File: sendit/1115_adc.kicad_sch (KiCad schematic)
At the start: 4 parts, among them U1 ADS1115IDGS

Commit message: big update on the potential design.
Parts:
- renumbered C1 to C2, C2 to C3, R2 to R6, U1 to U2
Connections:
- net +5V renamed +3.3V
- net GNDA renamed GND
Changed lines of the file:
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@@
 				)
 				(justify left)
-				(hide yes)
 			)
 		)
@@
 				)
 				(justify left)
-				(hide yes)
 			)
 		)
@@
 		(on_board yes)
 		(dnp no)
-		(property "Reference" "C2"
+		(property "Reference" "C3"
 			(at 176.53 88.9063 0)
 			(effects
@@
 		(instances
 			(project "sendit"
-				(path "/a355e4d0-2918-44fc-be8d-2503b84c6d6c/b74372e1-8e8c-456e-860f-c00883d6d009"
-					(reference "C4")
+				(path "/a355e4d0-2918-44fc-be8d-2503b84c6d6c/3be26641-bb38-49f4-a8c8-35d985e646a7"
+					(reference "C3")
 					(unit 1)
 				)
 				(path "/a355e4d0-2918-44fc-be8d-2503b84c6d6c/d44ed8a4-b2b5-49ad-a2f4-3423c838bfc7"
-					(reference "C2")
+					(reference "C8")
+					(unit 1)
+				)
+			)
+		)
+	)
+	(symbol
+		(lib_id "power:GND")
+		(at 132.08 107.95 0)
+		(unit 1)
+		(exclude_from_sim no)
+		(in_bom yes)
+		(on_board yes)
+		(dnp no)
+		(fields_autoplaced yes)
+		(property "Reference" "#PWR012"
+			(at 132.08 114.3 0)
+			(effects
+				(font
+					(size 1.27 1.27)
+				)
+				(hide yes)
+			)
+		)
+		(property "Value" "GND"
+			(at 132.08 113.03 0)
+			(effects
+				(font
+					(size 1.27 1.27)
+				)
+			)
+		)
+		(property "Footprint" ""
+			(at 132.08 107.95 0)
+			(effects
+				(font
+					(size 1.27 1.27)
+				)
+				(hide yes)
+			)
+		)
+		(property "Datasheet" ""
+			(at 132.08 107.95 0)
+			(effects
+				(font
+					(size 1.27 1.27)
+				)
+				(hide yes)
+			)
+		)
+		(property "Description" "Power symbol creates a global label with name \"GND\" , ground"
+			(at 132.08 107.95 0)
+			(effects
+				(font
+					(size 1.27 1.27)
+				)
+				(hide yes)
+			)
+		)
+		(pin "1"
+		)
+		(instances
+			(project "sendit"
+				(path "/a355e4d0-2918-44fc-be8d-2503b84c6d6c/3be26641-bb38-49f4-a8c8-35d985e646a7"
+					(reference "#PWR012")
+					(unit 1)
+				)
+				(path "/a355e4d0-2918-44fc-be8d-2503b84c6d6c/d44ed8a4-b2b5-49ad-a2f4-3423c838bfc7"
+					(reference "#PWR030")
 					(unit 1)
 				)
@@
 		(on_board yes)
 		(dnp no)
-		(property "Reference" "C1"
+		(property "Reference" "C2"
 			(at 163.83 88.9063 0)
 			(effects
@@
 		(instances
 			(project "sendit"
-				(path "/a355e4d0-2918-44fc-be8d-2503b84c6d6c/b74372e1-8e8c-456e-860f-c00883d6d009"
-					(reference "C3")
+				(path "/a355e4d0-2918-44fc-be8d-2503b84c6d6c/3be26641-bb38-49f4-a8c8-35d985e646a7"
+					(reference "C2")
 					(unit 1)
 				)
 				(path "/a355e4d0-2918-44fc-be8d-2503b84c6d6c/d44ed8a4-b2b5-49ad-a2f4-3423c838bfc7"
-					(reference "C1")
+					(reference "C7")
 					(unit 1)
 				)
@@
 		(dnp no)
 		(fields_autoplaced yes)
-		(property "Reference" "R2"
+		(property "Reference" "R6"
 			(at 153.67 81.28 0)
 			(effects
@@
 		(instances
 			(project "sendit"
-				(path "/a355e4d0-2918-44fc-be8d-2503b84c6d6c/b74372e1-8e8c-456e-860f-c00883d6d009"
-					(reference "R10")
+				(path "/a355e4d0-2918-44fc-be8d-2503b84c6d6c/3be26641-bb38-49f4-a8c8-35d985e646a7"
+					(reference "R6")
 					(unit 1)
 				)
 				(path "/a355e4d0-2918-44fc-be8d-2503b84c6d6c/d44ed8a4-b2b5-49ad-a2f4-3423c838bfc7"
-					(reference "R2")
+					(reference "R12")
 					(unit 1)
 				)
@@
 		(dnp no)
 		(fields_autoplaced yes)
-		(property "Reference" "U1"
+		(property "Reference" "U2"
 			(at 134.2741 80.01 0)
 			(effects
@@
 		(instances
 			(project "sendit"
-				(path "/a355e4d0-2918-44fc-be8d-2503b84c6d6c/b74372e1-8e8c-456e-860f-c00883d6d009"
-					(reference "U3")
+				(path "/a355e4d0-2918-44fc-be8d-2503b84c6d6c/3be26641-bb38-49f4-a8c8-35d985e646a7"
+					(reference "U2")
 					(unit 1)
 				)
 				(path "/a355e4d0-2918-44fc-be8d-2503b84c6d6c/d44ed8a4-b2b5-49ad-a2f4-3423c838bfc7"
-					(reference "U1")
+					(reference "U4")
 					(unit 1)
 				)
@@
 	)
 	(symbol
-		(lib_id "power:GNDA")
-		(at 132.08 107.95 0)
-		(unit 1)
-		(exclude_from_sim no)
-		(in_bom yes)
-		(on_board yes)
-		(dnp no)
-		(property "Reference" "#PWR03"
-			(at 132.08 114.3 0)
-			(effects
-				(font
-					(size 1.27 1.27)
-				)
-				(hide yes)
-			)
-		)
-		(property "Value" "GNDA"
-			(at 132.08 111.76 0)
-			(effects
-				(font
-					(size 1.27 1.27)
-				)
-			)
-		)
-		(property "Footprint" ""
-			(at 132.08 107.95 0)
-			(effects
-				(font
-					(size 1.27 1.27)
-				)
-				(hide yes)
-			)
-		)
-		(property "Datasheet" ""
-			(at 132.08 107.95 0)
-			(effects
-				(font
-					(size 1.27 1.27)
-				)
-				(hide yes)
-			)
-		)
-		(property "Description" "Power symbol creates a global label with name \"GNDA\" , analog ground"
-			(at 132.08 107.95 0)
-			(effects
-				(font
-					(size 1.27 1.27)
-				)
-				(hide yes)
-			)
-		)
-		(pin "1"
-		)
-		(instances
-			(project "sendit"
-				(path "/a355e4d0-2918-44fc-be8d-2503b84c6d6c/b74372e1-8e8c-456e-860f-c00883d6d009"
-					(reference "#PWR022")
-					(unit 1)
-				)
-				(path "/a355e4d0-2918-44fc-be8d-2503b84c6d6c/d44ed8a4-b2b5-49ad-a2f4-3423c838bfc7"
-					(reference "#PWR03")
-					(unit 1)
-				)
-			)
-		)
-	)
-	(symbol
-		(lib_id "power:+5V")
+		(lib_id "power:+3.3V")
 		(at 132.08 72.39 0)
 		(unit 1)
@@
 		(dnp no)
 		(fields_autoplaced yes)
-		(property "Reference" "#PWR02"
+		(property "Reference" "#PWR011"
 			(at 132.08 76.2 0)
 			(effects
@@
 			)
 		)
-		(property "Value" "+5V"
+		(property "Value" "+3.3V"
 			(at 132.08 67.31 0)
 			(effects
@@
 			)
 		)
-		(property "Description" "Power symbol creates a global label with name \"+5V\""
+		(property "Description" "Power symbol creates a global label with name \"+3.3V\""
 			(at 132.08 72.39 0)
 			(effects
@@
 		(instances
 			(project "sendit"
-				(path "/a355e4d0-2918-44fc-be8d-2503b84c6d6c/b74372e1-8e8c-456e-860f-c00883d6d009"
-					(reference "#PWR021")
+				(path "/a355e4d0-2918-44fc-be8d-2503b84c6d6c/3be26641-bb38-49f4-a8c8-35d985e646a7"
+					(reference "#PWR011")
 					(unit 1)
 				)
 				(path "/a355e4d0-2918-44fc-be8d-2503b84c6d6c/d44ed8a4-b2b5-49ad-a2f4-3423c838bfc7"
-					(reference "#PWR02")
-					(unit 1)
-				)
+					(reference "#PWR029")
+					(unit 1)
+				)

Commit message: layout work.
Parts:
- renumbered R6 to R9
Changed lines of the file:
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@@
 				)
 				(path "/a355e4d0-2918-44fc-be8d-2503b84c6d6c/d44ed8a4-b2b5-49ad-a2f4-3423c838bfc7"
-					(reference "C8")
+					(reference "C7")
 					(unit 1)
 				)
@@
 		(dnp no)
 		(fields_autoplaced yes)
-		(property "Reference" "#PWR012"
+		(property "Reference" "#PWR019"
 			(at 132.08 114.3 0)
 			(effects
@@
 			(project "sendit"
 				(path "/a355e4d0-2918-44fc-be8d-2503b84c6d6c/3be26641-bb38-49f4-a8c8-35d985e646a7"
-					(reference "#PWR012")
-					(unit 1)
-				)
-				(path "/a355e4d0-2918-44fc-be8d-2503b84c6d6c/d44ed8a4-b2b5-49ad-a2f4-3423c838bfc7"
-					(reference "#PWR030")
+					(reference "#PWR019")
+					(unit 1)
+				)
+				(path "/a355e4d0-2918-44fc-be8d-2503b84c6d6c/d44ed8a4-b2b5-49ad-a2f4-3423c838bfc7"
+					(reference "#PWR043")
 					(unit 1)
 				)
@@
 				)
 				(path "/a355e4d0-2918-44fc-be8d-2503b84c6d6c/d44ed8a4-b2b5-49ad-a2f4-3423c838bfc7"
-					(reference "C7")
+					(reference "C6")
 					(unit 1)
 				)
@@
 		(dnp no)
 		(fields_autoplaced yes)
-		(property "Reference" "R6"
+		(property "Reference" "R9"
 			(at 153.67 81.28 0)
 			(effects
@@
 			(project "sendit"
 				(path "/a355e4d0-2918-44fc-be8d-2503b84c6d6c/3be26641-bb38-49f4-a8c8-35d985e646a7"
-					(reference "R6")
-					(unit 1)
-				)
-				(path "/a355e4d0-2918-44fc-be8d-2503b84c6d6c/d44ed8a4-b2b5-49ad-a2f4-3423c838bfc7"
-					(reference "R12")
+					(reference "R9")
+					(unit 1)
+				)
+				(path "/a355e4d0-2918-44fc-be8d-2503b84c6d6c/d44ed8a4-b2b5-49ad-a2f4-3423c838bfc7"
+					(reference "R26")
 					(unit 1)
 				)
@@
 				)
 				(path "/a355e4d0-2918-44fc-be8d-2503b84c6d6c/d44ed8a4-b2b5-49ad-a2f4-3423c838bfc7"
-					(reference "U4")
+					(reference "U3")
 					(unit 1)
 				)
@@
 		(dnp no)
 		(fields_autoplaced yes)
-		(property "Reference" "#PWR011"
+		(property "Reference" "#PWR018"
 			(at 132.08 76.2 0)
 			(effects
@@
 			(project "sendit"
 				(path "/a355e4d0-2918-44fc-be8d-2503b84c6d6c/3be26641-bb38-49f4-a8c8-35d985e646a7"
-					(reference "#PWR011")
-					(unit 1)
-				)
-				(path "/a355e4d0-2918-44fc-be8d-2503b84c6d6c/d44ed8a4-b2b5-49ad-a2f4-3423c838bfc7"
-					(reference "#PWR029")
-					(unit 1)
-				)
+					(reference "#PWR018")
+					(unit 1)
+				)
+				(path "/a355e4d0-2918-44fc-be8d-2503b84c6d6c/d44ed8a4-b2b5-49ad-a2f4-3423c838bfc7"
+					(reference "#PWR042")
+					(unit 1)
+				)

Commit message: updated footprints and lcsc numbers.
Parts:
- C2: footprint Capacitor_SMD:C_0805_2012Metric_Pad1.18x1.45mm_HandSolder -> Capacitor_SMD:C_0603_1608Metric; LCSC C49678 -> C14663
- C3: footprint Capacitor_SMD:C_0805_2012Metric_Pad1.18x1.45mm_HandSolder -> Capacitor_SMD:C_0603_1608Metric; LCSC C1952580 -> C19702
- R9: footprint Resistor_SMD:R_0805_2012Metric_Pad1.20x1.40mm_HandSolder -> Resistor_SMD:R_0603_1608Metric; LCSC C84376 -> (none)
- U2: LCSC (none) -> C37593
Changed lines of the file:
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@@
 			)
 		)
-		(property "Footprint" "Capacitor_SMD:C_0805_2012Metric_Pad1.18x1.45mm_HandSolder"
+		(property "Footprint" "Capacitor_SMD:C_0603_1608Metric"
 			(at 173.99 90.17 0)
 			(effects
@@
 			)
 		)
-		(property "LCSC" "C1952580"
+		(property "LCSC" "C19702"
 			(at 173.99 90.17 0)
 			(effects
@@
 			)
 		)
-		(property "Footprint" "Capacitor_SMD:C_0805_2012Metric_Pad1.18x1.45mm_HandSolder"
+		(property "Footprint" "Capacitor_SMD:C_0603_1608Metric"
 			(at 161.29 90.17 0)
 			(effects
@@
 			)
 		)
-		(property "LCSC" "C49678"
+		(property "LCSC" "C14663"
 			(at 161.29 90.17 0)
 			(effects
@@
 			)
 		)
-		(property "Footprint" "Resistor_SMD:R_0805_2012Metric_Pad1.20x1.40mm_HandSolder"
+		(property "Footprint" "Resistor_SMD:R_0603_1608Metric"
 			(at 151.13 82.55 0)
 			(effects
@@
 			)
 		)
-		(property "LCSC" "C84376"
+		(property "LCSC" ""
 			(at 151.13 82.55 0)
 			(effects
@@
 			)
 		)
-		(property "LCSC" ""
+		(property "LCSC" "C37593"
 			(at 132.08 95.25 0)
 			(effects

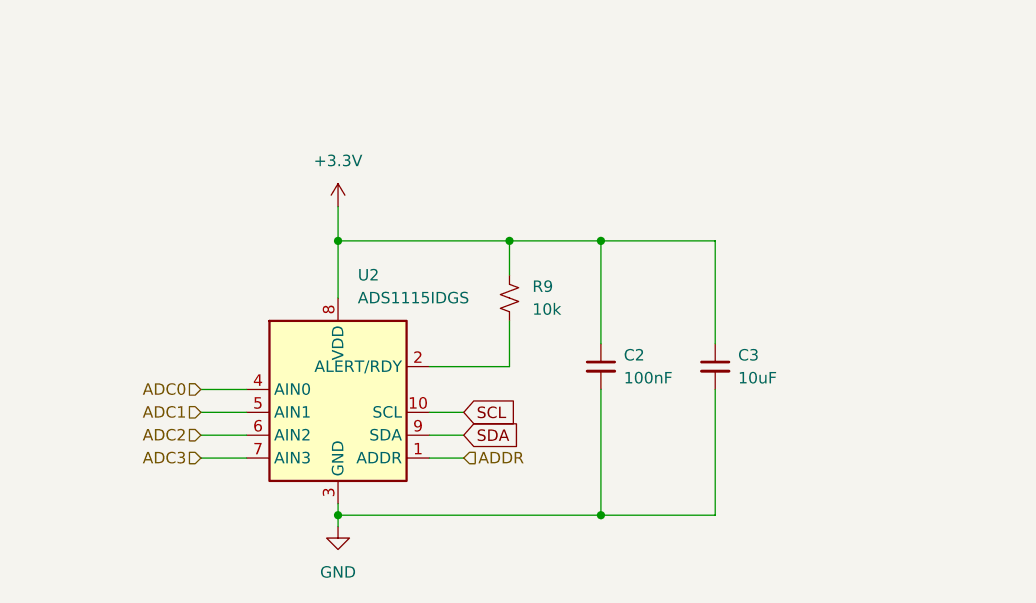
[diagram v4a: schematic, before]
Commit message: test run of jlcpcb upload looks good.
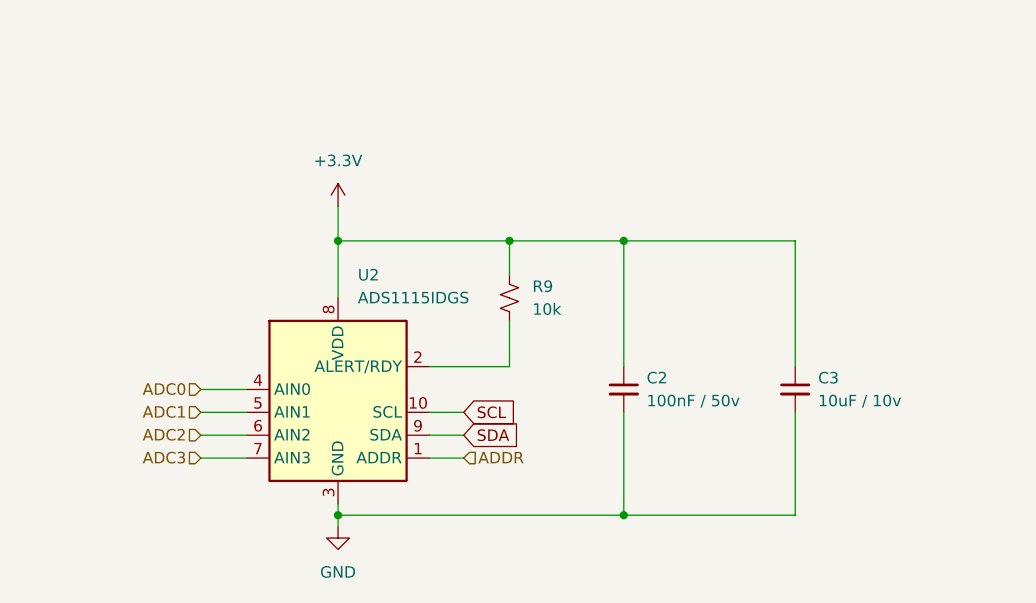
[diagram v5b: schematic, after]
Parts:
- C2: value 100nF -> 100nF / 50v
- C3: value 10uF -> 10uF / 10v
- R9: LCSC (none) -> C25804
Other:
- moved on the sheet: C2, C3
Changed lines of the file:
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@@
 	)
 	(junction
-		(at 161.29 106.68)
+		(at 163.83 106.68)
 		(diameter 0)
 		(color 0 0 0 0)
 	)
 	(junction
-		(at 161.29 76.2)
+		(at 163.83 76.2)
 		(diameter 0)
 		(color 0 0 0 0)
@@
 	(wire
 		(pts
-			(xy 161.29 106.68) (xy 132.08 106.68)
+			(xy 132.08 106.68) (xy 163.83 106.68)
 		)
 		(stroke
@@
 	(wire
 		(pts
-			(xy 161.29 76.2) (xy 173.99 76.2)
-		)
-		(stroke
-			(width 0)
-			(type default)
-		)
-	)
-	(wire
-		(pts
 			(xy 116.84 97.79) (xy 121.92 97.79)
 		)
@@
 	(wire
 		(pts
-			(xy 173.99 106.68) (xy 161.29 106.68)
+			(xy 182.88 106.68) (xy 163.83 106.68)
 		)
 		(stroke
@@
 	(wire
 		(pts
-			(xy 161.29 92.71) (xy 161.29 106.68)
+			(xy 163.83 95.25) (xy 163.83 106.68)
 		)
 		(stroke
@@
 	(wire
 		(pts
-			(xy 173.99 92.71) (xy 173.99 106.68)
-		)
-		(stroke
-			(width 0)
-			(type default)
-		)
-	)
-	(wire
-		(pts
-			(xy 151.13 76.2) (xy 161.29 76.2)
+			(xy 182.88 95.25) (xy 182.88 106.68)
+		)
+		(stroke
+			(width 0)
+			(type default)
+		)
+	)
+	(wire
+		(pts
+			(xy 151.13 76.2) (xy 163.83 76.2)
 		)
 		(stroke
@@
 	(wire
 		(pts
-			(xy 161.29 76.2) (xy 161.29 87.63)
-		)
-		(stroke
-			(width 0)
-			(type default)
-		)
-	)
-	(wire
-		(pts
-			(xy 173.99 76.2) (xy 173.99 87.63)
+			(xy 163.83 76.2) (xy 163.83 90.17)
+		)
+		(stroke
+			(width 0)
+			(type default)
+		)
+	)
+	(wire
+		(pts
+			(xy 182.88 76.2) (xy 182.88 90.17)
 		)
 		(stroke
@@
 		(pts
 			(xy 142.24 90.17) (xy 151.13 90.17)
+		)
+		(stroke
+			(width 0)
+			(type default)
+		)
+	)
+	(wire
+		(pts
+			(xy 163.83 76.2) (xy 182.88 76.2)
 		)
 		(stroke
@@
 	(symbol
 		(lib_id "Device:C_Small")
-		(at 173.99 90.17 0)
+		(at 182.88 92.71 0)
 		(unit 1)
 		(exclude_from_sim no)
@@
 		(dnp no)
 		(property "Reference" "C3"
-			(at 176.53 88.9063 0)
+			(at 185.42 91.4463 0)
 			(effects
 				(font
@@
 			)
 		)
-		(property "Value" "10uF"
-			(at 176.53 91.4463 0)
+		(property "Value" "10uF / 10v"
+			(at 185.42 93.9863 0)
 			(effects
 				(font
@@
 		)
 		(property "Footprint" "Capacitor_SMD:C_0603_1608Metric"
-			(at 173.99 90.17 0)
+			(at 182.88 92.71 0)
 			(effects
 				(font
@@
 		)
 		(property "Datasheet" "~"
-			(at 173.99 90.17 0)
+			(at 182.88 92.71 0)
 			(effects
 				(font
@@
 		)
 		(property "Description" ""
-			(at 173.99 90.17 0)
+			(at 182.88 92.71 0)
 			(effects
 				(font
@@
 		)
 		(property "Vendor" ""
-			(at 173.99 90.17 0)
+			(at 182.88 92.71 0)
 			(effects
 				(font
@@
 		)
 		(property "LCSC" "C19702"
-			(at 173.99 90.17 0)
+			(at 182.88 92.71 0)
 			(effects
 				(font
@@
 	(symbol
 		(lib_id "Device:C_Small")
-		(at 161.29 90.17 0)
+		(at 163.83 92.71 0)
 		(unit 1)
 		(exclude_from_sim no)
@@
 		(dnp no)
 		(property "Reference" "C2"
-			(at 163.83 88.9063 0)
+			(at 166.37 91.4463 0)
 			(effects
 				(font
@@
 			)
 		)
-		(property "Value" "100nF"
-			(at 163.83 91.4463 0)
+		(property "Value" "100nF / 50v"
+			(at 166.37 93.9863 0)
 			(effects
 				(font
@@
 		)
 		(property "Footprint" "Capacitor_SMD:C_0603_1608Metric"
-			(at 161.29 90.17 0)
+			(at 163.83 92.71 0)
 			(effects
 				(font
@@
 		)
 		(property "Datasheet" "~"
-			(at 161.29 90.17 0)
+			(at 163.83 92.71 0)
 			(effects
 				(font
@@
 		)
 		(property "Description" ""
-			(at 161.29 90.17 0)
+			(at 163.83 92.71 0)
 			(effects
 				(font
@@
 		)
 		(property "Mouser" ""
-			(at 161.29 90.17 0)
+			(at 163.83 92.71 0)
 			(effects
 				(font
@@
 		)
 		(property "LCSC" "C14663"
-			(at 161.29 90.17 0)
+			(at 163.83 92.71 0)
 			(effects
 				(font
@@
 			)
 		)
-		(property "LCSC" ""
+		(property "LCSC" "C25804"
 			(at 151.13 82.55 0)
 			(effects

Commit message: added alert lines
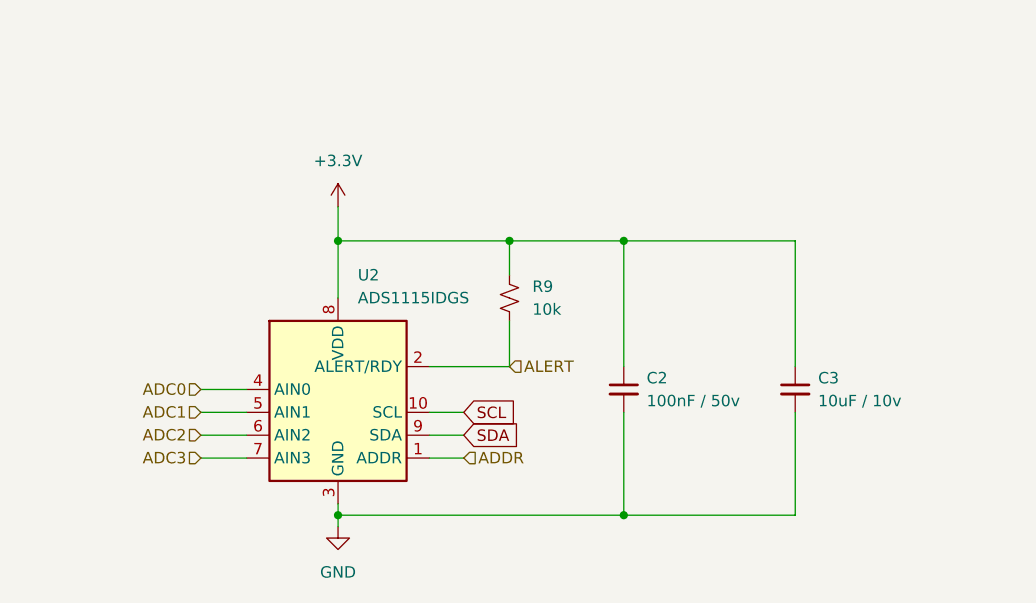
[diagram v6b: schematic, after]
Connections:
- net ALERT: now reaches R9.1, U2.2 (ALERT/RDY)
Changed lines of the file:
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@@
+		)
+	)
+	(hierarchical_label "ALERT"
+		(shape input)
+		(at 151.13 90.17 0)
+		(effects
+			(font
+				(size 1.27 1.27)
+			)
+			(justify left)
 		)
 	)

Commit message: started work on the rev c schematic
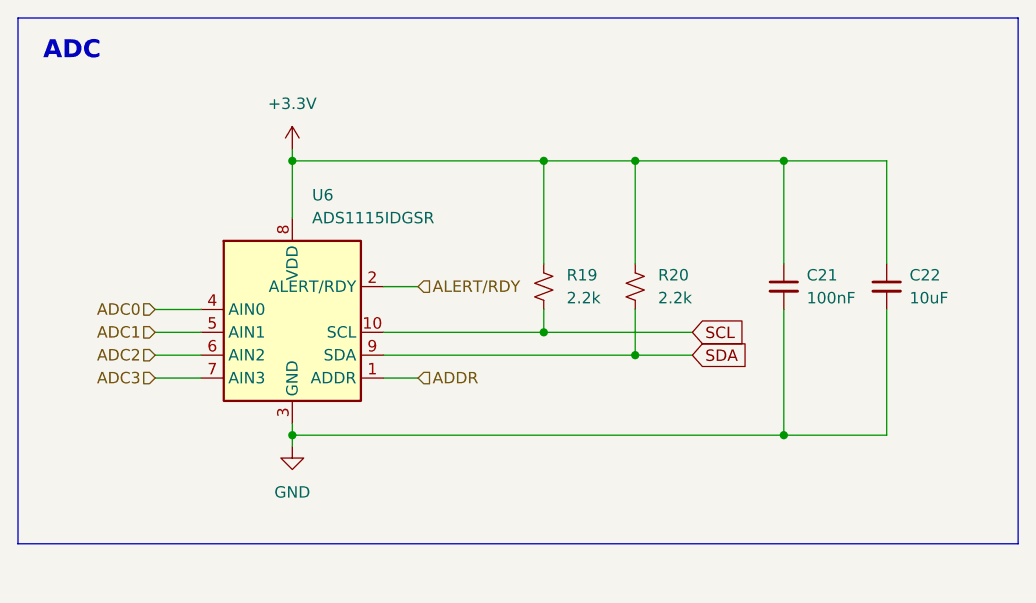
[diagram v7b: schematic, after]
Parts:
- removed C2: 100nF / 50v, Capacitor_SMD:C_0603_1608Metric, symbol Device:C_Small
- removed C3: 10uF / 10v, Capacitor_SMD:C_0603_1608Metric, symbol Device:C_Small
- removed R9: 10k, Resistor_SMD:R_0603_1608Metric, symbol Device:R_Small_US
- removed U2: ADS1115IDGS, Package_SO:TSSOP-10_3x3mm_P0.5mm, symbol Analog_ADC:ADS1015IDGS
- added C21: 100nF, Capacitor_SMD:C_0603_1608Metric, symbol Device:C_Small
- added C22: 10uF, Capacitor_SMD:C_0603_1608Metric, symbol Device:C_Small
- added R19, R20: 2.2k, Resistor_SMD:R_0603_1608Metric, symbol Device:R_Small_US
- added U6: ADS1115IDGSR, Package_SO:TSSOP-10_3x3mm_P0.5mm, symbol Analog_ADC:ADS1115IDGS
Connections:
- net +3.3V: now also C21.1, C22.1, R19.2, R20.2, U6.8 (VDD)
- net ADC0: now also U6.4 (AIN0)
- net ADC1: now also U6.5 (AIN1)
- net ADC2: now also U6.6 (AIN2)
- net ADC3: now also U6.7 (AIN3)
- net ADDR: now also U6.1 (ADDR)
- net GND: now also C21.2, C22.2, U6.3 (GND)
- net SCL: now also R19.1, U6.10 (SCL)
- net SDA: now also R20.1, U6.9 (SDA)
- new net ALERT/RDY: U6.2 (ALERT/RDY)
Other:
- note added: "ADC"
- title: (none) -> https://github.com/hoeken/brineomatic

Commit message: most of the work on the schematic is done.
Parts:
- renumbered C21 to C20, C22 to C21, U6 to U7
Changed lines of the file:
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@@
 		(on_board yes)
 		(dnp no)
-		(property "Reference" "C21"
+		(property "Reference" "C20"
 			(at 184.15 80.0163 0)
 			(effects
@@
 				)
 				(path "/a355e4d0-2918-44fc-be8d-2503b84c6d6c/8b22d84f-0b54-48cc-b723-35a0934e8e0a"
-					(reference "C21")
+					(reference "C20")
 					(unit 1)
 				)
@@
 		(on_board yes)
 		(dnp no)
-		(property "Reference" "C22"
+		(property "Reference" "C21"
 			(at 195.58 80.0163 0)
 			(effects
@@
 				)
 				(path "/a355e4d0-2918-44fc-be8d-2503b84c6d6c/8b22d84f-0b54-48cc-b723-35a0934e8e0a"
-					(reference "C22")
+					(reference "C21")
 					(unit 1)
 				)
@@
 		(dnp no)
 		(fields_autoplaced yes)
-		(property "Reference" "#PWR020"
+		(property "Reference" "#PWR023"
 			(at 127 69.85 0)
 			(effects
@@
 			(project "sendit"
 				(path "/a355e4d0-2918-44fc-be8d-2503b84c6d6c/8455ca3a-09fb-49d0-8692-dd30220f1ed8"
+					(reference "#PWR038")
+					(unit 1)
+				)
+				(path "/a355e4d0-2918-44fc-be8d-2503b84c6d6c/8b22d84f-0b54-48cc-b723-35a0934e8e0a"
 					(reference "#PWR023")
-					(unit 1)
-				)
-				(path "/a355e4d0-2918-44fc-be8d-2503b84c6d6c/8b22d84f-0b54-48cc-b723-35a0934e8e0a"
-					(reference "#PWR020")
 					(unit 1)
 				)
@@
 			(project "sendit"
 				(path "/a355e4d0-2918-44fc-be8d-2503b84c6d6c/8455ca3a-09fb-49d0-8692-dd30220f1ed8"
-					(reference "R21")
+					(reference "R30")
 					(unit 1)
 				)
@@
 		(dnp no)
 		(fields_autoplaced yes)
-		(property "Reference" "U6"
+		(property "Reference" "U7"
 			(at 129.1941 71.12 0)
 			(effects
@@
 			(project "sendit"
 				(path "/a355e4d0-2918-44fc-be8d-2503b84c6d6c/8455ca3a-09fb-49d0-8692-dd30220f1ed8"
-					(reference "U10")
+					(reference "U8")
 					(unit 1)
 				)
 				(path "/a355e4d0-2918-44fc-be8d-2503b84c6d6c/8b22d84f-0b54-48cc-b723-35a0934e8e0a"
-					(reference "U6")
+					(reference "U7")
 					(unit 1)
 				)
@@
 		(dnp no)
 		(fields_autoplaced yes)
-		(property "Reference" "#PWR021"
+		(property "Reference" "#PWR024"
 			(at 127 105.41 0)
 			(effects
@@
 			(project "sendit"
 				(path "/a355e4d0-2918-44fc-be8d-2503b84c6d6c/8455ca3a-09fb-49d0-8692-dd30220f1ed8"
+					(reference "#PWR039")
+					(unit 1)
+				)
+				(path "/a355e4d0-2918-44fc-be8d-2503b84c6d6c/8b22d84f-0b54-48cc-b723-35a0934e8e0a"
 					(reference "#PWR024")
-					(unit 1)
-				)
-				(path "/a355e4d0-2918-44fc-be8d-2503b84c6d6c/8b22d84f-0b54-48cc-b723-35a0934e8e0a"
-					(reference "#PWR021")
 					(unit 1)
 				)
@@
 			(project "sendit"
 				(path "/a355e4d0-2918-44fc-be8d-2503b84c6d6c/8455ca3a-09fb-49d0-8692-dd30220f1ed8"
-					(reference "R22")
-					(unit 1)
-				)
+					(reference "R31")
+					(unit 1)
+				)
